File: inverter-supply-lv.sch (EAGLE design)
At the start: 61 parts, among them IC3 1039-2387**3.3V 300mA LDO Vol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, U1 1039-2397** MP2456GJ-Z 0.5A, 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, U2 1039-9015**AOZ1282CI Buck Swi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, X1 0289-9066**15EDGVC-3.81-02P-14

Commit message: Girise fuse eklendi.
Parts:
- added F1: (no value), adafruit:PTCFUSE-1206
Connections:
- net N$55: now also F1.1
- net N$6: now also F1.2
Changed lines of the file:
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@@
 <part name="SUPPLY13" library="supply2" library_urn="urn:adsk.eagle:library:372" deviceset="DGND" device=""/>
 <part name="SUPPLY14" library="supply2" library_urn="urn:adsk.eagle:library:372" deviceset="DGND" device=""/>
+<part name="F1" library="adafruit" library_urn="urn:adsk.eagle:library:420" deviceset="PTCFUSE" device="-1206" package3d_urn="urn:adsk.eagle:package:6240569/1"/>
 </parts>
 <sheets>
@@
 <instance part="SUPPLY14" gate="G$1" x="436.88" y="22.86" smashed="yes">
 <attribute name="VALUE" x="436.245" y="30.607" size="1.778" layer="96" rot="R270"/>
+</instance>
+<instance part="F1" gate="G$1" x="16.51" y="97.79" smashed="yes">
+<attribute name="VALUE" x="12.7" y="96.52" size="1.778" layer="96"/>
+<attribute name="NAME" x="12.7" y="102.87" size="1.778" layer="95"/>
 </instance>
 </instances>
@@
 <segment>
 <wire x1="25.4" y1="96.52" x2="25.4" y2="100.33" width="0.1524" layer="91"/>
-<wire x1="25.4" y1="100.33" x2="21.5646" y2="100.33" width="0.1524" layer="91"/>
+<wire x1="25.4" y1="100.33" x2="21.59" y2="100.33" width="0.1524" layer="91"/>
 <pinref part="B1" gate="G$1" pin="AC1"/>
+<wire x1="21.59" y1="100.33" x2="21.5646" y2="100.33" width="0.1524" layer="91"/>
 <wire x1="25.4" y1="100.33" x2="36.83" y2="100.33" width="0.1524" layer="91"/>
 <wire x1="36.83" y1="100.33" x2="36.83" y2="96.52" width="0.1524" layer="91"/>
+<pinref part="F1" gate="G$1" pin="2"/>
+<junction x="21.59" y="100.33"/>
 </segment>
 </net>
@@
 <wire x1="11.43" y1="100.33" x2="6.35" y2="100.33" width="0.1524" layer="91"/>
 <pinref part="X1" gate=".2" pin="SK"/>
-</segment>
-</net>
+<pinref part="F1" gate="G$1" pin="1"/>
+</segment>
+</net>

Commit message: Bitti
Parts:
- removed C104: 1200920268**CAP 0603 CER 100nF 50V %10 X7R, rcl:C-EUC0603E
- removed C84: 1200920252**CAP 0603 CER 1nF 50V %10 X7R, rcl:C-EUC0603E
- added C3: 1019-1016**CAP 1210 CER 10uF 50V %10 X7R (Sadece Murata kul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, ercl:C-EUC1210
- added C8: 1200920268**CAP 0603 CER 100nF 50V %10 X7R, rcl:C-EUC0603E
- C29: value 1200920268**CAP 0603 CER 100nF 50V %10 X7R -> 1200920252**CAP 0603 CER 1nF 50V %10 X7R
- C4: value 1019-1016**CAP 1210 CER 10uF 50V %10 X7R (Sadece Murata kullanylabilir) -> 10uF 50V %10 X7R; device ercl:C-EUC1210 -> rcl:C-EUC0805E
- C6: value 10uF 50V %10 X7R -> 1200920268**CAP 0603 CER 100nF 50V %10 X7R; device rcl:C-EUC0805E -> rcl:C-EUC0603E
- renumbered C102 to C13, C103 to C5, C105 to C7, C106 to C12, C108 to C15, C109 to C16, C110 to C17, C111 to C25, C112 to C26, C113 to C9, C30 to C14, C32 to C10, C48 to C18, C49 to C24, C60 to C20, C69 to C23, C70 to C11, C72 to C22, C78 to C27, C80 to C28, C98 to C19, C99 to C21, D11 to D1, D18 to D4, D25 to D2, D26 to D3, D27 to D5, IC3 to IC1, LED6 to LED2, R133 to R9, R134 to R10, R135 to R11, R138 to R13, R182 to R14, R190 to R1, R191 to R6, R192 to R2, R193 to R7, R194 to R8, R195 to R12, R61 to R3, R62 to R4, R63 to R5
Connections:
- net +3V3: now also C29.1; no longer C84.1
- net DGND: now also C29.2, C3.1; no longer C104.1, C84.2
- net N$11: now also C8.2; no longer C29.2
- net N$35: now also C8.1; no longer C29.1
- net N$72: now also C3.2; no longer C104.2
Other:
- moved on the sheet: C29, C4, C6

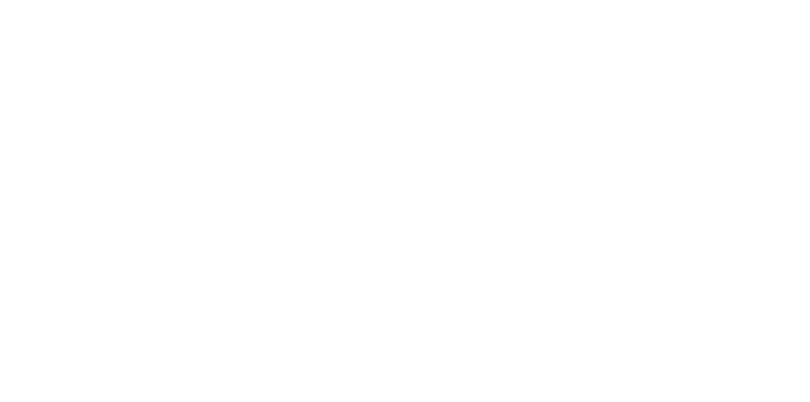
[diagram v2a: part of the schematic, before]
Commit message: Tutturma pad'leri eklendi, soketler icin aciklayici text'ler eklendi.
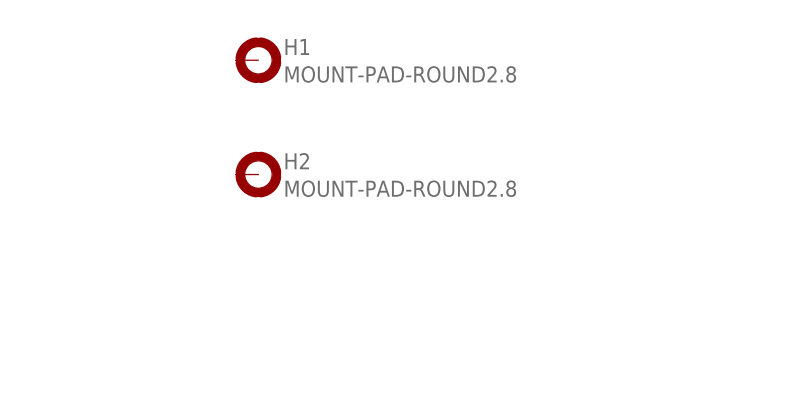
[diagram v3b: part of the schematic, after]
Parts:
- added H1, H2: MOUNT-PAD-ROUND2.8, holes:MOUNT-PAD-ROUND2.8
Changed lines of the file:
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@@
 <part name="SUPPLY14" library="supply2" library_urn="urn:adsk.eagle:library:372" deviceset="DGND" device=""/>
 <part name="F1" library="adafruit" library_urn="urn:adsk.eagle:library:420" deviceset="PTCFUSE" device="-1206" package3d_urn="urn:adsk.eagle:package:6240569/1"/>
+<part name="H1" library="holes" library_urn="urn:adsk.eagle:library:237" deviceset="MOUNT-PAD-ROUND" device="2.8" package3d_urn="urn:adsk.eagle:package:14281/1"/>
+<part name="H2" library="holes" library_urn="urn:adsk.eagle:library:237" deviceset="MOUNT-PAD-ROUND" device="2.8" package3d_urn="urn:adsk.eagle:package:14281/1"/>
 </parts>
 <sheets>
@@
 <attribute name="NAME" x="12.7" y="102.87" size="1.778" layer="95"/>
 </instance>
+<instance part="H1" gate="G$1" x="71.12" y="185.42" smashed="yes">
+<attribute name="NAME" x="73.914" y="186.0042" size="1.778" layer="95"/>
+<attribute name="VALUE" x="73.914" y="182.9562" size="1.778" layer="96"/>
+</instance>
+<instance part="H2" gate="G$1" x="71.12" y="172.72" smashed="yes">
+<attribute name="NAME" x="73.914" y="173.3042" size="1.778" layer="95"/>
+<attribute name="VALUE" x="73.914" y="170.2562" size="1.778" layer="96"/>
+</instance>
 </instances>

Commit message: Malzeme degerlerinde degisiklikler yapilmisti sanirim.
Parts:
- R13: value 1200970927**RES 0603 100R %1 1/10W -> 470R
- R14: value 1029-2006**RES 0603 47R %1 -> 220R
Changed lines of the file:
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@@
 <part name="C10" library="rcl" deviceset="C-EU" device="C0603E" value="1200920268**CAP 0603 CER 100nF 50V %10 X7R"/>
 <part name="LED1" library="led" deviceset="LED" device="CHIP-LED0805" value="1200960006**DIODE LED SMD 0805 RED 10mcd 638nm AlInGaP"/>
-<part name="R13" library="rcl" deviceset="R-EU_" device="R0603E" value="1200970927**RES 0603 100R %1 1/10W"/>
+<part name="R13" library="rcl" deviceset="R-EU_" device="R0603E" value="470R"/>
 <part name="IC1" library="enko" deviceset="NCP115ASN330T2G" device="" value="1039-2387**3.3V 300mA LDO Voltage Regulator TSOP-5"/>
 <part name="C18" library="rcl" deviceset="C-EU" device="C0603E" value="1200920268**CAP 0603 CER 100nF 50V %10 X7R"/>
@@
 <part name="C19" library="rcl" deviceset="C-EU" device="C0603E" value="1200920252**CAP 0603 CER 1nF 50V %10 X7R"/>
 <part name="C21" library="rcl" deviceset="C-EU" device="C0603E" value="1019-3387**CAP 0603 CER 10uF 10V %10 X5R"/>
-<part name="R14" library="rcl" deviceset="R-EU_" device="R0603E" value="1029-2006**RES 0603 47R %1"/>
+<part name="R14" library="rcl" deviceset="R-EU_" device="R0603E" value="220R"/>
 <part name="LED2" library="led" deviceset="LED" device="CHIP-LED0805" value="1200960006**DIODE LED SMD 0805 RED 10mcd 638nm AlInGaP"/>
 <part name="C11" library="rcl" deviceset="C-EU" device="C0805E" value="10uF 50V %10 X7R"/>
